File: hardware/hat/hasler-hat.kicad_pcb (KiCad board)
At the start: 4 copper layers, 85 x 41 mm, 112 parts, among them J1 Amp4 top header, J2 Hasler J2, J3 USB-C PD in, J4 Debug / expansion, J5 Qwiic, J6 To Amp4 DC in, Q1 AO4407A, Q2 2N7002, U1 MCP23017, U10 SRV05-4, U11 SRV05-4, U12 SRV05-4, U2 ADS1115, U3 CH224A, U4 LM393, U5 AZ431AN, U6 XC6206P332MR, U7 SRV05-4, U8 SRV05-4, U9 SRV05-4

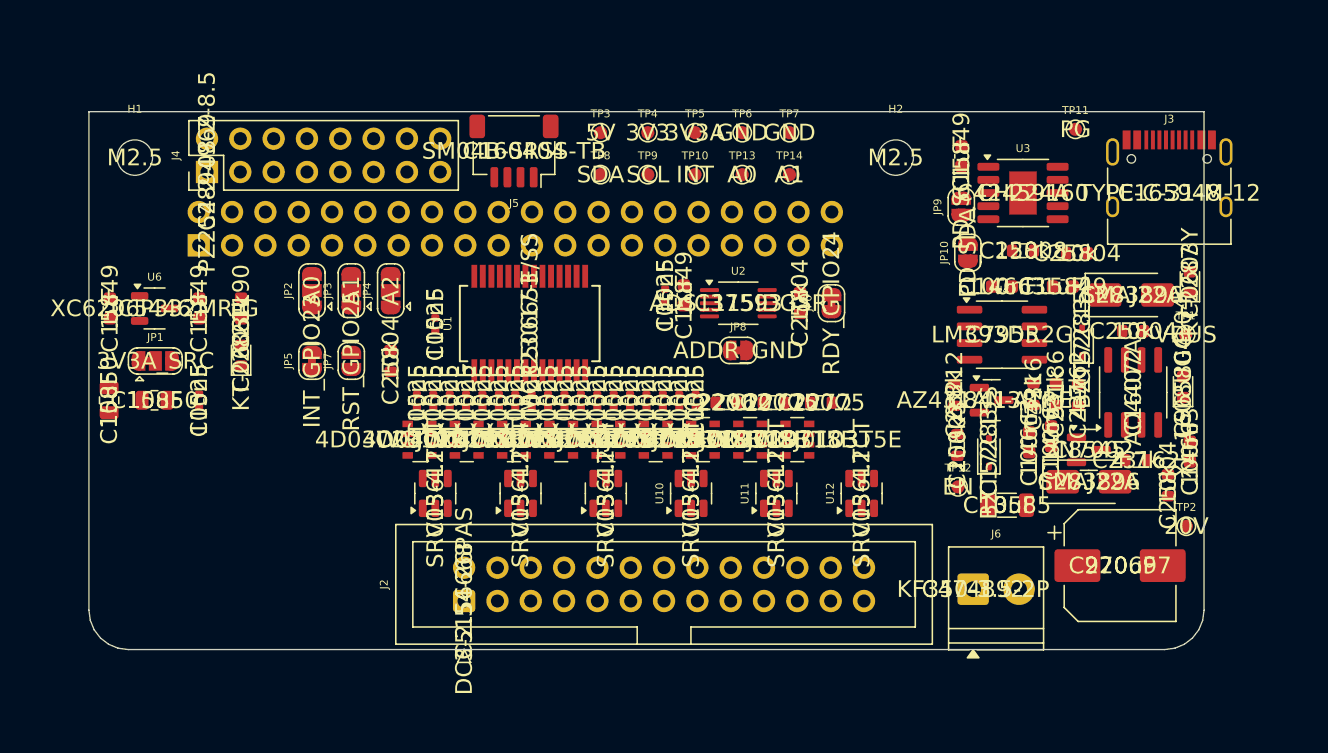
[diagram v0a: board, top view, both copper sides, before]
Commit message: HAT: 85 mm board, power column placement, net classes, fab script, ordering note
Co-Authored-By: Claude Opus 5.5 <noreply@anthropic.com>
Claude-Session: https://claude.ai/code/session_014wovV18Ypx4LXt9k8BSCRk
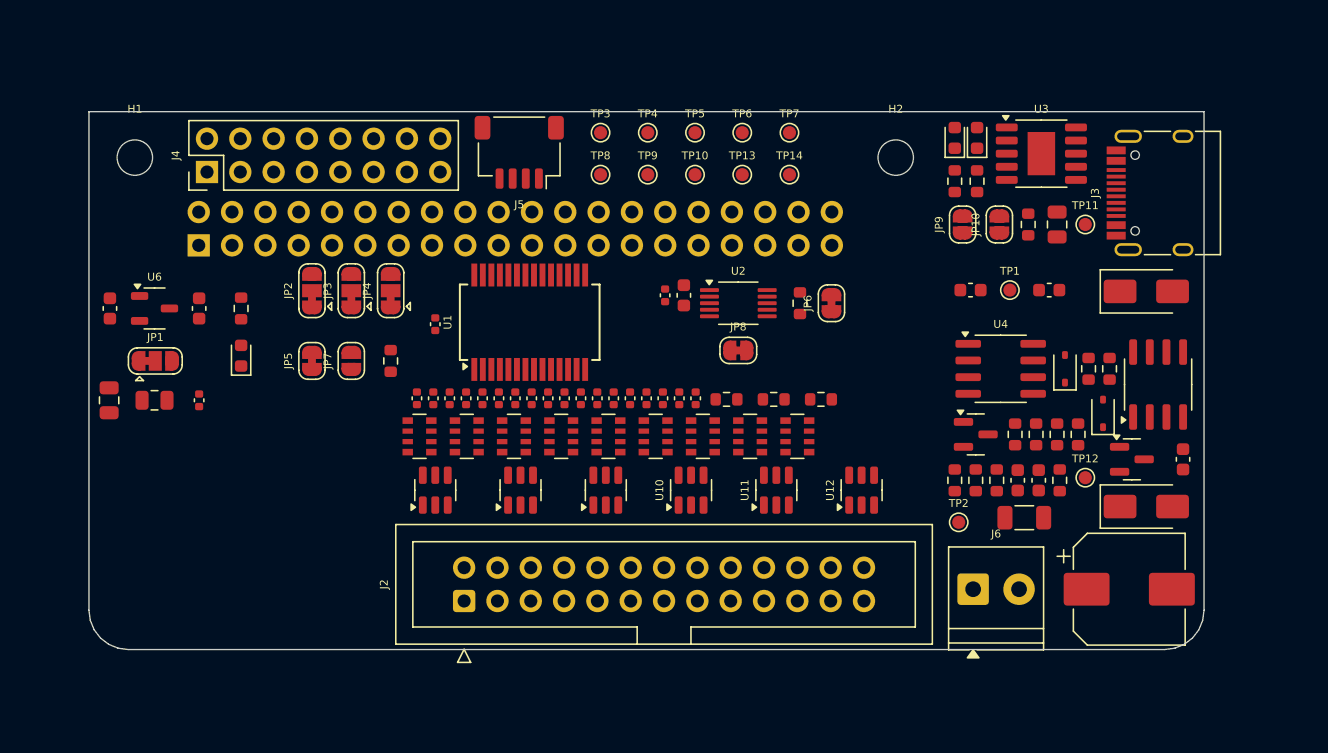
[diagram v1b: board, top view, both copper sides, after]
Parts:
- added R14: 10k, Resistor_SMD:R_0603_1608Metric, F.Cu at (173.8, 124.6)
- added R15: 4.7k, Resistor_SMD:R_0603_1608Metric, F.Cu at (169.2, 128.1)
- added R16: 1M, Resistor_SMD:R_0603_1608Metric, F.Cu at (175.4, 124.6)
- C1: footprint Capacitor_SMD:C_0603_1608Metric -> Capacitor_SMD:C_0805_2012Metric
- C3, C4: value 100nF -> 1nF
- R5: value 5.1k -> 33k
- R6: value 4.7k -> 5.1k
- R8: value 4.7k -> 2.2k
- R9: value 10k -> 4.7k
- moved R10 27.4 mm to (167.7, 105.3)
- moved D6 24.6 mm to (167.7, 102.0)
- moved D2 21.0 mm to (166.0, 102.0)
- moved TP2 17.4 mm to (166.3, 131.3)
- moved TP1 13.8 mm to (170.2, 113.6)
- moved R2 10.8 mm to (166.0, 105.3), turned to 90 degrees
- moved R6 10.2 mm to (167.6, 128.1)
- moved R5 10.1 mm to (166.0, 128.1)
- moved TP12 9.73 mm to (175.9, 127.9)
- moved D3 9.20 mm to (177.3, 123.0)
- moved C1 8.95 mm to (173.8, 108.6)
- moved R7 8.25 mm to (174.0, 128.1)
- moved TP11 7.29 mm to (175.9, 108.6)
- moved R8 7.26 mm to (177.8, 119.6), turned to 90 degrees
- moved R3 5.51 mm to (170.6, 124.6)
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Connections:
- R5 pad 1: DIV_UV -> VBUS
- R5 pad 2: DIV_OV -> DIV_OVT
- R6 pad 1: DIV_OV -> DIV_OVT
- R6 pad 2: GND -> DIV_OV
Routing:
- added copper zone on In1.Cu, net GND

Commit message: HAT: complete routing - GND fan-out before routing, pre-routed power paths, VOUT trunk, notch for the Amp4 cap, gap closer; pull-ups to the cabinet side
Co-Authored-By: Claude Opus 5.5 <noreply@anthropic.com>
Claude-Session: https://claude.ai/code/session_014wovV18Ypx4LXt9k8BSCRk
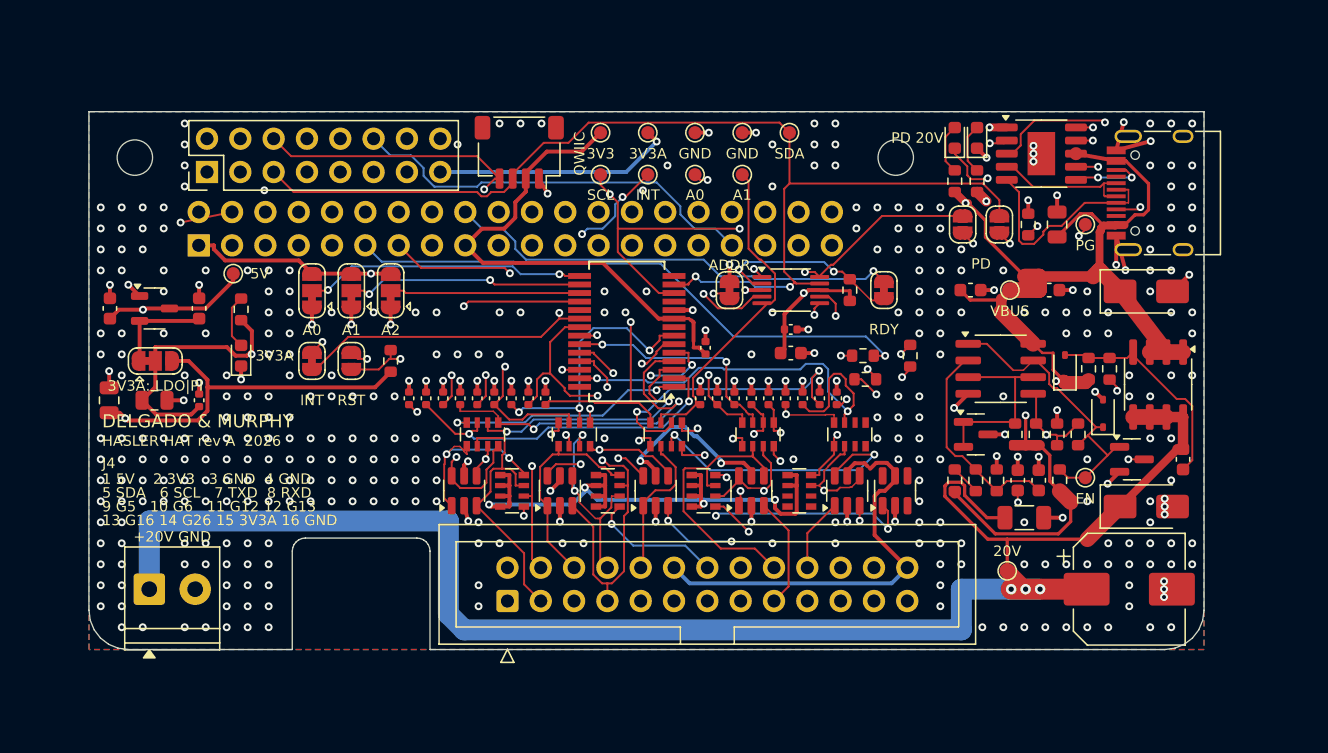
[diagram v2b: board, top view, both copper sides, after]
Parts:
- moved J6 62.8 mm to (104.6, 136.4)
- moved TP3 30.0 mm to (111.0, 112.3)
- moved RN4 22.0 mm to (158.0, 124.6), turned to 90 degrees
- moved C14 20.7 mm to (147.0, 118.0)
- moved RN3 18.6 mm to (151.0, 124.6), turned to 90 degrees
- moved TP8 14.8 mm to (153.4, 101.6)
- moved C33 13.2 mm to (154.4, 121.8)
- moved C32 13.1 mm to (153.1, 121.8)
- moved C31 13.1 mm to (151.8, 121.8)
- moved C30 13.0 mm to (150.5, 121.8)
- moved C29 12.9 mm to (149.2, 121.8)
- moved C28 12.9 mm to (147.9, 121.8)
- moved RN6 11.7 mm to (132.2, 128.9)
- moved R20 10.9 mm to (159.0, 118.6)
- moved C37 10.8 mm to (157.0, 121.8)
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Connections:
- net +3V3 renamed /+3V3
- net +5V renamed /+5V
- net 3V3A renamed /3V3A
- net ADS_ADDR renamed /ADS_ADDR
- net ADS_RDY renamed /ADS_RDY
- net CC1 renamed /CC1
- net CC2 renamed /CC2
- net DIV_OV renamed /DIV_OV
- net DIV_OVT renamed /DIV_OVT
- net DIV_UV renamed /DIV_UV
- net EN renamed /EN
- net GATE_PULL renamed /GATE_PULL
- net GND renamed /GND
- net GPIO12 renamed /GPIO12
- net GPIO13 renamed /GPIO13
- net GPIO16 renamed /GPIO16
- net GPIO17 renamed /GPIO17
- net GPIO22 renamed /GPIO22
- net GPIO23 renamed /GPIO23
- net GPIO24 renamed /GPIO24
- net GPIO25 renamed /GPIO25
- net GPIO26 renamed /GPIO26
- net GPIO27 renamed /GPIO27
- net GPIO5 renamed /GPIO5
- net GPIO6 renamed /GPIO6
- net J_LB renamed /J_LB
- net J_LG renamed /J_LG
- net J_LR renamed /J_LR
- net LDO_OUT renamed /LDO_OUT
- net LED_3V3 renamed /LED_3V3
- net LED_OUT renamed /LED_OUT
- net LED_PD renamed /LED_PD
- net MCP_A0 renamed /MCP_A0
- net MCP_A1 renamed /MCP_A1
- net MCP_A2 renamed /MCP_A2
- net MCP_INTA renamed /MCP_INTA
- net MCP_RST renamed /MCP_RST
- net PD_CFG1 renamed /PD_CFG1
- net PD_PG renamed /PD_PG
- net PD_SCL renamed /PD_SCL
- net PD_SDA renamed /PD_SDA
- net PGATE renamed /PGATE
- net RXD renamed /RXD
- net SCL renamed /SCL
- net SDA renamed /SDA
- net TXD renamed /TXD
- net USB_DM renamed /USB_DM
- net USB_DP renamed /USB_DP
- net VBUS renamed /VBUS
- net VOUT renamed /VOUT
- net VREF renamed /VREF
- C20 pad 1: M_K1 -> /M_K1
- C21 pad 1: M_K2 -> /M_K2
- C22 pad 1: M_K3 -> /M_K3
- C23 pad 1: M_K4 -> /M_K4
- C24 pad 1: M_K5 -> /M_K5
- C25 pad 1: M_K6 -> /M_K6
- C26 pad 1: M_PU -> /M_PU
- C27 pad 1: M_A0 -> /M_TSW
- C28 pad 1: M_A1 -> /M_X1
- C29 pad 1: M_TSW -> /M_X2
- C30 pad 1: M_X1 -> /M_X3
- C31 pad 1: M_X2 -> /M_X4
- C32 pad 1: M_X3 -> /M_X5
- C33 pad 1: M_X4 -> /M_X6
- C34 pad 1: M_X5 -> /M_A0
- C35 pad 1: M_X6 -> /M_A1
- C36 pad 1: M_A2 -> /M_A2
- C37 pad 1: M_A3 -> /M_A3
- J1 pad 12: (no net) -> unconnected-(J1-Pin_12-Pad12)
- J1 pad 19: (no net) -> unconnected-(J1-Pin_19-Pad19)
- J1 pad 21: (no net) -> unconnected-(J1-Pin_21-Pad21)
- J1 pad 23: (no net) -> unconnected-(J1-Pin_23-Pad23)
- J1 pad 24: (no net) -> unconnected-(J1-Pin_24-Pad24)
- J1 pad 26: (no net) -> unconnected-(J1-Pin_26-Pad26)
- J1 pad 27: (no net) -> unconnected-(J1-Pin_27-Pad27)
- J1 pad 28: (no net) -> unconnected-(J1-Pin_28-Pad28)
- J1 pad 35: (no net) -> unconnected-(J1-Pin_35-Pad35)
- J1 pad 38: (no net) -> unconnected-(J1-Pin_38-Pad38)
- J1 pad 40: (no net) -> unconnected-(J1-Pin_40-Pad40)
- J1 pad 7: (no net) -> unconnected-(J1-Pin_7-Pad7)
- J2 pad 1: J_K1 -> /J_K1
- J2 pad 10: J_A1 -> /J_A1
- J2 pad 14: J_TSW -> /J_TSW
- J2 pad 17: J_X1 -> /J_X1
- J2 pad 18: J_X2 -> /J_X2
- J2 pad 19: J_X3 -> /J_X3
- J2 pad 20: J_X4 -> /J_X4
- J2 pad 21: J_X5 -> /J_X5
- J2 pad 22: J_X6 -> /J_X6
- J2 pad 23: J_A2 -> /J_A2
- J2 pad 25: J_A3 -> /J_A3
- J2 pad 3: J_K2 -> /J_K2
- J2 pad 4: J_K3 -> /J_K3
- J2 pad 5: J_K4 -> /J_K4
- J2 pad 6: J_K5 -> /J_K5
- J2 pad 7: J_K6 -> /J_K6
- J2 pad 8: J_PU -> /J_PU
- J2 pad 9: J_A0 -> /J_A0
- J3 pad A8: (no net) -> unconnected-(J3-SBU1-PadA8)
- J3 pad B8: (no net) -> unconnected-(J3-SBU2-PadB8)
- RN1 pad 1: J_K1 -> /J_K1
- RN1 pad 2: J_K2 -> /J_K2
- RN1 pad 3: J_K3 -> /J_K3
- RN1 pad 4: J_K4 -> /J_K4
- RN1 pad 5: M_K4 -> /M_K4
- RN1 pad 6: M_K3 -> /M_K3
- RN1 pad 7: M_K2 -> /M_K2
- RN1 pad 8: M_K1 -> /M_K1
- RN2 pad 1: J_K5 -> /J_K5
- RN2 pad 2: J_K6 -> /J_K6
- RN2 pad 3: J_PU -> /J_PU
- RN2 pad 4: J_A0 -> /J_TSW
- RN2 pad 5: M_A0 -> /M_TSW
- RN2 pad 6: M_PU -> /M_PU
- RN2 pad 7: M_K6 -> /M_K6
- RN2 pad 8: M_K5 -> /M_K5
- RN3 pad 1: J_A1 -> /J_X1
- RN3 pad 2: J_TSW -> /J_X2
- RN3 pad 3: J_X1 -> /J_X3
- RN3 pad 4: J_X2 -> /J_X4
- RN3 pad 5: M_X2 -> /M_X4
- RN3 pad 6: M_X1 -> /M_X3
- RN3 pad 7: M_TSW -> /M_X2
- RN3 pad 8: M_A1 -> /M_X1
- RN4 pad 1: J_X3 -> /J_X5
- RN4 pad 2: J_X4 -> /J_X6
- RN4 pad 3: J_X5 -> unconnected-(RN4-R3.1-Pad3)
- RN4 pad 4: J_X6 -> unconnected-(RN4-R4.1-Pad4)
- RN4 pad 5: M_X6 -> unconnected-(RN4-R4.2-Pad5)
- RN4 pad 6: M_X5 -> unconnected-(RN4-R3.2-Pad6)
- RN4 pad 7: M_X4 -> /M_X6
- RN4 pad 8: M_X3 -> /M_X5
- RN5 pad 1: J_A2 -> /J_A0
- RN5 pad 2: J_A3 -> /J_A1
- RN5 pad 3: (no net) -> /J_A2
- RN5 pad 4: (no net) -> /J_A3
- RN5 pad 5: (no net) -> /M_A3
- RN5 pad 6: (no net) -> /M_A2
- RN5 pad 7: M_A3 -> /M_A1
- RN5 pad 8: M_A2 -> /M_A0
- RN6 pad 5: M_K4 -> /J_K4
- RN6 pad 6: M_K3 -> /J_K3
- RN6 pad 7: M_K2 -> /J_K2
- RN6 pad 8: M_K1 -> /J_K1
- RN7 pad 5: M_TSW -> /J_TSW
- RN7 pad 6: M_PU -> /J_PU
- RN7 pad 7: M_K6 -> /J_K6
- RN7 pad 8: M_K5 -> /J_K5
- RN8 pad 5: M_X4 -> /J_X4
- RN8 pad 6: M_X3 -> /J_X3
- RN8 pad 7: M_X2 -> /J_X2
- RN8 pad 8: M_X1 -> /J_X1
- RN9 pad 3: (no net) -> unconnected-(RN9-R3.1-Pad3)
- RN9 pad 4: (no net) -> unconnected-(RN9-R4.1-Pad4)
- RN9 pad 5: (no net) -> unconnected-(RN9-R4.2-Pad5)
- RN9 pad 6: (no net) -> unconnected-(RN9-R3.2-Pad6)
- RN9 pad 7: M_X6 -> /J_X6
- RN9 pad 8: M_X5 -> /J_X5
- TP13 pad 1: M_A0 -> /M_A0
- TP14 pad 1: M_A1 -> /M_A1
- U1 pad 1: M_K1 -> /M_K1
- U1 pad 11: (no net) -> unconnected-(U1-NC-Pad11)
- U1 pad 14: (no net) -> unconnected-(U1-NC-Pad14)
- U1 pad 19: (no net) -> unconnected-(U1-INTB-Pad19)
- U1 pad 2: M_K2 -> /M_K2
- U1 pad 21: M_TSW -> /M_TSW
- U1 pad 22: M_X1 -> /M_X1
- U1 pad 23: M_X2 -> /M_X2
- U1 pad 24: M_X3 -> /M_X3
- U1 pad 25: M_X4 -> /M_X4
- U1 pad 26: M_X5 -> /M_X5
- U1 pad 27: M_X6 -> /M_X6
- U1 pad 28: (no net) -> unconnected-(U1-GPA7-Pad28)
- U1 pad 3: M_K3 -> /M_K3
- U1 pad 4: M_K4 -> /M_K4
- U1 pad 5: M_K5 -> /M_K5
- U1 pad 6: M_K6 -> /M_K6
- U1 pad 7: M_PU -> /M_PU
- U1 pad 8: (no net) -> unconnected-(U1-GPB7-Pad8)
- U10 pad 3: J_X1 -> /J_X1
- U10 pad 4: J_X2 -> /J_X2
- U10 pad 6: J_X3 -> /J_X3
- U11 pad 1: J_X4 -> /J_X4
- U11 pad 3: J_X5 -> /J_X5
- U11 pad 4: J_X6 -> /J_X6
- U11 pad 6: J_A2 -> /J_A2
- U12 pad 1: J_A3 -> /J_A3
- U12 pad 3: (no net) -> unconnected-(U12-IO2-Pad3)
- U12 pad 4: (no net) -> unconnected-(U12-IO3-Pad4)
- U12 pad 6: (no net) -> unconnected-(U12-IO4-Pad6)
- U2 pad 4: M_A0 -> /M_A0
- U2 pad 5: M_A1 -> /M_A1
- U2 pad 6: M_A2 -> /M_A2
- U2 pad 7: M_A3 -> /M_A3
- U7 pad 1: J_K1 -> /J_K1
- U7 pad 3: J_K2 -> /J_K2
- U7 pad 4: J_K3 -> /J_K3
- U7 pad 6: J_K4 -> /J_K4
- U8 pad 1: J_K5 -> /J_K5
- U8 pad 3: J_K6 -> /J_K6
- U8 pad 4: J_PU -> /J_PU
- U8 pad 6: J_A0 -> /J_A0
- U9 pad 1: J_A1 -> /J_A1
- U9 pad 4: J_TSW -> /J_TSW
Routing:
- net /3V3A: track 0.00 -> 188.0 mm, vias 0 -> 7
- net /+3V3: track 0.00 -> 184.7 mm, vias 0 -> 6
- net /VOUT: track 0.00 -> 162.0 mm, vias 0 -> 4
- net /VBUS: track 0.00 -> 97.8 mm, vias 0 -> 4
- net /SDA: track 0.00 -> 95.4 mm, vias 0 -> 2
- net /SCL: track 0.00 -> 81.5 mm, vias 0 -> 4
- net /GND: track 0.00 -> 72.1 mm, vias 0 -> 386
- net /J_LG: track 0.00 -> 49.9 mm, vias 0 -> 2
- net /GPIO22: track 0.00 -> 47.7 mm, vias 0 -> 1
- net /GPIO27: track 0.00 -> 44.6 mm, vias 0 -> 2
- net /GPIO17: track 0.00 -> 44.0 mm, vias 0 -> 1
- net /M_A0: track 0.00 -> 37.3 mm, vias 0 -> 3
- net /MCP_INTA: track 0.00 -> 36.6 mm, vias 0 -> 3
- net /J_TSW: track 0.00 -> 35.2 mm, vias 0 -> 2
- net /GPIO24: track 0.00 -> 34.9 mm, vias 0 -> 1
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- added copper zone on B.Cu, net /GND
- added copper zone on F.Cu, net /GND
- added copper zone on In2.Cu, net /GND
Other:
- outline, holes or cut-outs redrawn
- board text added: "+20V GND"
- board text added: "1 5V 2 3V3 3 GND 4 GND"
- board text added: "1 K1 / key 1"
- board text added: "10 volume"
- board text added: "11 pots GND"
- board text added: "12 3V3A (pots, LED +)"
- board text added: "13 G16 14 G26 15 3V3A 16 GND"
- board text added: "13 LED red"
- board text added: "14 tone sw / key 0"
- board text added: "15 LED green"
- board text added: "16 LED blue"
- board text added: "17 - / Tape"
- board text added: "18 - / SP"
- board text added: "19 - / spk a"
- board text added: "2 GND"
- board text added: "20 - / spk b"
- board text added: "20V"
- board text added: "21 spare"
- board text added: "22 spare"
- board text added: "23 - / bass"
- board text added: "24 GND"
- board text added: "25 spare analog"
- board text added: "26 3V3A"
- board text added: "3 K2 / key 2"
- board text added: "3V3"
- board text added: "3V3A"
- board text added: "3V3A: LDO|PI"
- board text added: "4 K3 / key 3"
- board text added: "5 K4 / key 4"
- board text added: "5 SDA 6 SCL 7 TXD 8 RXD"
- board text added: "5V"
- board text added: "6 K5 / key 5"
- board text added: "7 K6 / key 6"
- board text added: "8 PU / Q"
- board text added: "9 G5 10 G6 11 G12 12 G13"
- board text added: "9 tone / treble"
- board text added: "A0"
- board text added: "A1"
- board text added: "A2"
- board text added: "ADDR"
- board text added: "DELGADO & MURPHY"
- board text added: "EN"
- board text added: "GND"
- board text added: "HASLER HAT rev A 2026"
- board text added: "Hasler HAT rev A - USB-C PD 20 V for the Amp4 Pro"
- board text added: "I2C: MCP23017 0x20 ADS1115 0x48 AMP 0x4D CH224A 0x22 (JP9/10)"
- board text added: "INT"
- board text added: "J2 HASLER (IDC, DIN 41651 - wire 1 = stripe = pin 1, key slot to the edge)"
- board text added: "J4"
- board text added: "J6 -> Amp4 Pro power terminal, + to +. Do not also use the Amp4 DC jack."
- board text added: "JLCJLCJLCJLC"
- board text added: "Never configure 28 V (CH224A). Window passes 10.8-22.8 V only."
- board text added: "PD"
- board text added: "PD 20V"
- board text added: "PG"
- board text added: "QWIIC"
- board text added: "RDY"
- board text added: "RST"
- board text added: "SCL"
- board text added: "SDA"
- board text added: "VBUS"

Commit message: HAT: DRC clean (0 violations, parity), power paths pre-routed and widened, silkscreen, black-mask renders, fab outputs
Co-Authored-By: Claude Opus 5.5 <noreply@anthropic.com>
Claude-Session: https://claude.ai/code/session_014wovV18Ypx4LXt9k8BSCRk
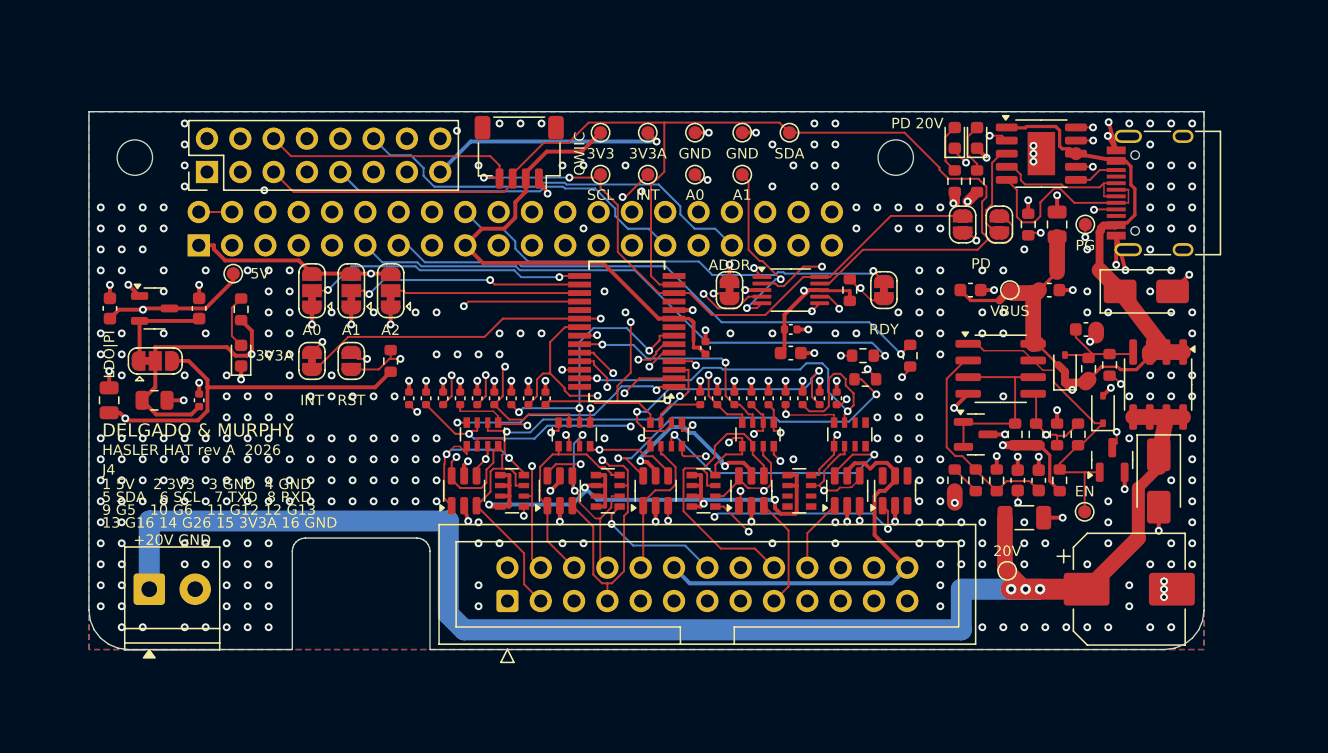
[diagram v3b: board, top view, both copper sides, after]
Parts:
- moved C6 12.4 mm to (176.0, 116.6), turned to 0 degrees
- moved TP12 2.60 mm to (175.9, 130.5)
- moved D5 2.17 mm to (181.6, 128.2), turned to -90 degrees
- moved Q2 1.50 mm to (178.0, 126.5), turned to 90 degrees
- moved D3 0.30 mm to (177.3, 122.7)
- moved R8 0.30 mm to (177.8, 119.3)
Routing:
- net /PD_SDA: track 26.2 -> 7.52 mm, vias 2 -> 0
- net /SDA: track 95.4 -> 107.3 mm, vias 2 -> 0
- net /PGATE: track 16.9 -> 7.88 mm
- net /VOUT: track 162.0 -> 153.2 mm, vias 4 -> 5
- net /SCL: track 81.5 -> 76.3 mm, vias 4 -> 2
- net /GPIO22: track 47.7 -> 43.1 mm
- net /VBUS: track 97.8 -> 101.8 mm
- net /M_A1: track 26.0 -> 29.9 mm, vias 0 -> 3
- net /J_LR: track 32.8 -> 36.4 mm, vias 3 -> 2
- net /M_K5: track 27.7 -> 24.3 mm, vias 4 -> 3
- net /PD_CFG1: track 14.4 -> 11.0 mm
- net /+5V: track 29.3 -> 26.2 mm, vias 2 -> 1
- net /J_X1: track 25.9 -> 28.8 mm, vias 2 -> 1
- net /ADS_RDY: track 14.8 -> 12.3 mm
- net /CC2: track 5.83 -> 3.38 mm, vias 2 -> 0
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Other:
- board text added: "+ to +. Leave the Amp4 DC"
- board text added: "ADS1115 0x48 AMP 0x4D"
- board text added: "CH224A 0x22 (JP9/JP10)"
- board text added: "Hasler HAT rev A 2026"
- board text added: "I2C MCP23017 0x20"
- board text added: "J2 (IDC) wire 1 = pin 1"
- board text added: "J6 -> Amp4 Pro power terminal,"
- board text added: "LDO|PI"
- board text added: "Never set the CH224A to 28 V."
- board text added: "Window passes 10.8-22.8 V."
- board text added: "jack empty."
- board text removed: "3V3A: LDO|PI"
- board text removed: "Hasler HAT rev A - USB-C PD 20 V for the Amp4 Pro"
- board text removed: "I2C: MCP23017 0x20 ADS1115 0x48 AMP 0x4D CH224A 0x22 (JP9/10)"
- board text removed: "J2 HASLER (IDC, DIN 41651 - wire 1 = stripe = pin 1, key slot to the edge)"
- board text removed: "J6 -> Amp4 Pro power terminal, + to +. Do not also use the Amp4 DC jack."
- board text removed: "Never configure 28 V (CH224A). Window passes 10.8-22.8 V only."
